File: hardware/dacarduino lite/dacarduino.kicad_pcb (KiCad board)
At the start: 2 copper layers, 95 x 67 mm, 41 parts, among them J11 CV IN, J12 CV IN, J13 CV IN, J17 VCC, J18 Vin, J3 CV OUT A, J4 CV OUT B, J5 GATE OUT A, J7 GATE IN, Q1 2N3904, Q3 2N3904, U1 MCP4922, U2 TL972

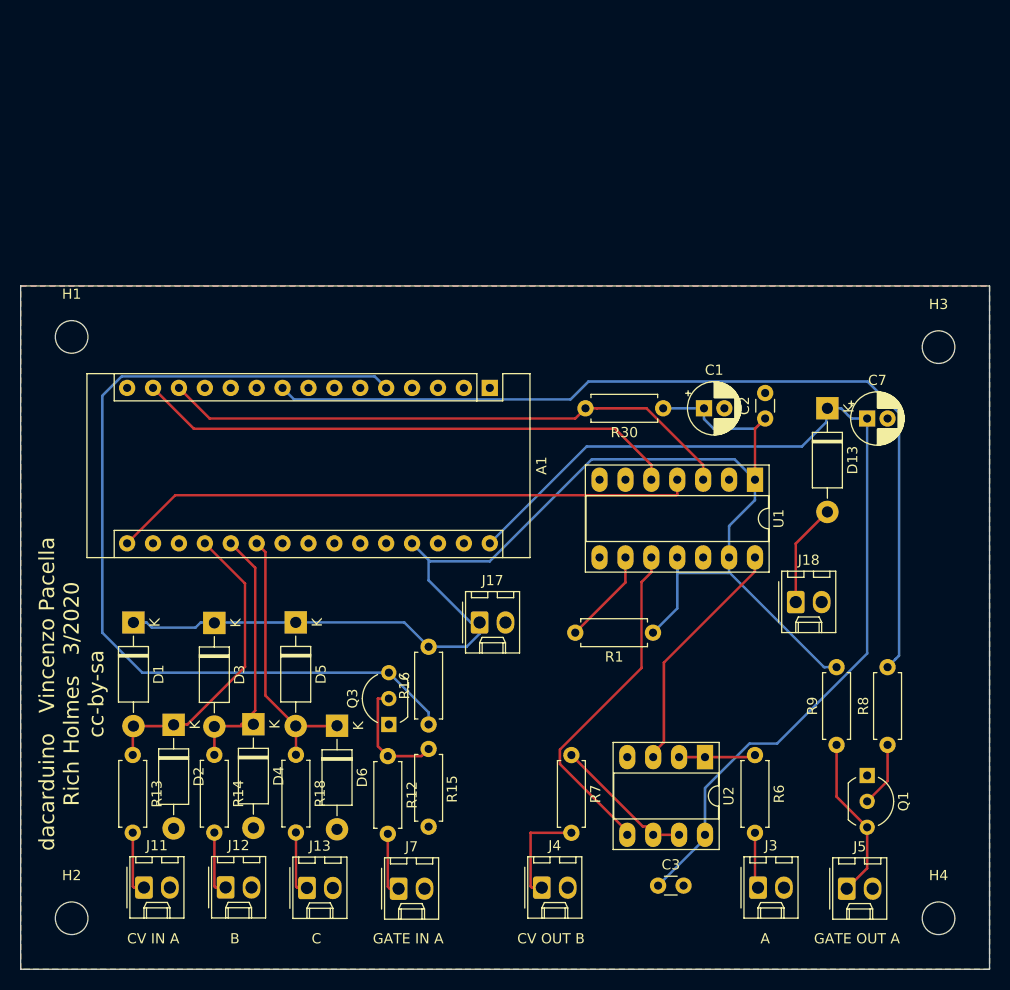
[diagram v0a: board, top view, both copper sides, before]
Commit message: Revised layout, with voltage reference restored to dacarduino
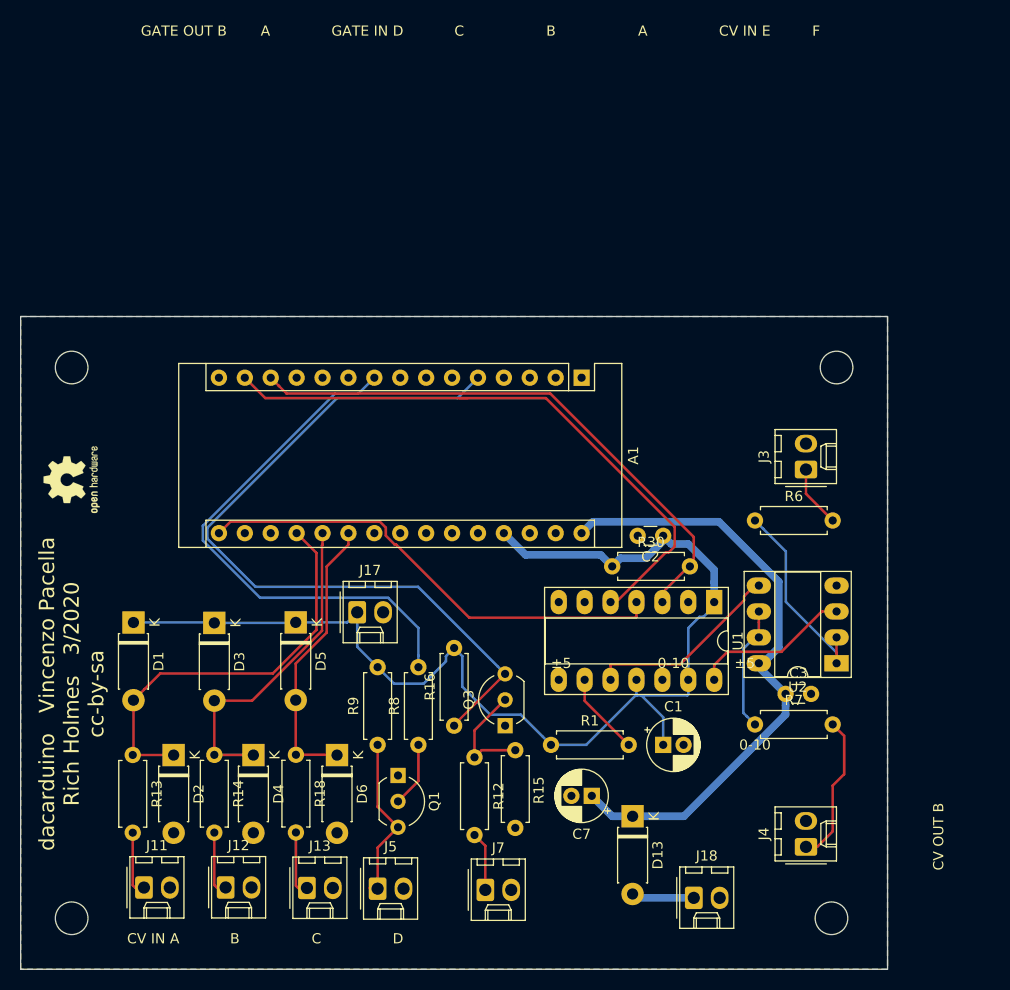
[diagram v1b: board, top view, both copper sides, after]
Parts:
- added REF**: OSHW-Logo2_7.3x6mm_SilkScreen, Symbol:OSHW-Logo2_7.3x6mm_SilkScreen, F.Cu at (130.0, 107.0)
- D1, D13, D2, D3, D4, D5, D6: footprint Diode_THT:D_DO-41_SOD81_P10.16mm_Horizontal -> Diode_THT:D_DO-41_SOD81_P7.62mm_Horizontal
- moved J5 46.0 mm to (160.0, 147.1)
- moved Q1 46.0 mm to (162.0, 136.0)
- moved R8 46.0 mm to (164.0, 133.0)
- moved C7 45.8 mm to (181.0, 138.0), turned to 180 degrees
- moved R9 45.0 mm to (160.0, 133.0)
- moved D13 44.3 mm to (185.0, 140.0)
- moved J3 41.3 mm to (202.0, 106.0), turned to 90 degrees
- moved C1 33.2 mm to (188.0, 133.0)
- moved J18 30.7 mm to (191.0, 148.0)
- moved J4 26.2 mm to (202.0, 143.0), turned to 90 degrees
- moved R6 23.0 mm to (197.0, 111.0), turned to 0 degrees
- moved C3 22.6 mm to (200.0, 128.0)
- moved R7 18.2 mm to (197.0, 131.0), turned to 0 degrees
- moved R30 16.3 mm to (183.0, 115.5), turned to 0 degrees
- moved U2 15.8 mm to (205.0, 125.0), turned to 180 degrees
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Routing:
- net +12V: track 99.5 -> 61.6 mm
- net /Arduino/D_OUT_A: track 88.3 -> 52.8 mm
- net VCC: track 142.8 -> 115.4 mm
- net /CV out/DAC_B: track 33.6 -> 20.0 mm
- net /Arduino/D_IN_A: track 88.7 -> 75.5 mm
- net Net-(R6-Pad1): track 7.52 -> 19.9 mm
- net /Arduino/A_IN_A: track 30.0 -> 40.5 mm
- net /Arduino/SCK: track 57.4 -> 47.2 mm
- net /CV out/DAC_A: track 24.3 -> 15.6 mm
- net /Arduino/MOSI: track 53.6 -> 59.5 mm
- net /Arduino/A_IN_B: track 27.6 -> 32.1 mm
- net /CV out/CV_OUT_B: track 10.3 -> 14.7 mm
- net Net-(D13-Pad2): track 10.1 -> 6.16 mm
- net /Arduino/DAC_CS: track 57.3 -> 55.6 mm
- net /Arduino/A_IN_C: track 26.4 -> 27.9 mm
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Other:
- board size 95 x 67 mm -> 85 x 64 mm
- board text added: "0-10"
- board text added: "CV IN E"
- board text added: "D"
- board text added: "F"
- board text added: "GATE IN D"
- board text added: "GATE OUT B"
- board text added: "±5"
- board text removed: "GATE IN A"
- board text removed: "GATE OUT A"
